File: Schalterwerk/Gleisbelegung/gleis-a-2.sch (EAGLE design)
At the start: 24 parts, among them Q1 P-MOSFET, Q2 P-MOSFET, X1 PHNX_4P_508CONN_1017493, X3 IO-HAT, X4 RJ45-JACK, X5 PHNX_4P_350CONN_1984989_PXC, X6 PHNX_4P_350CONN_1984989_PXC

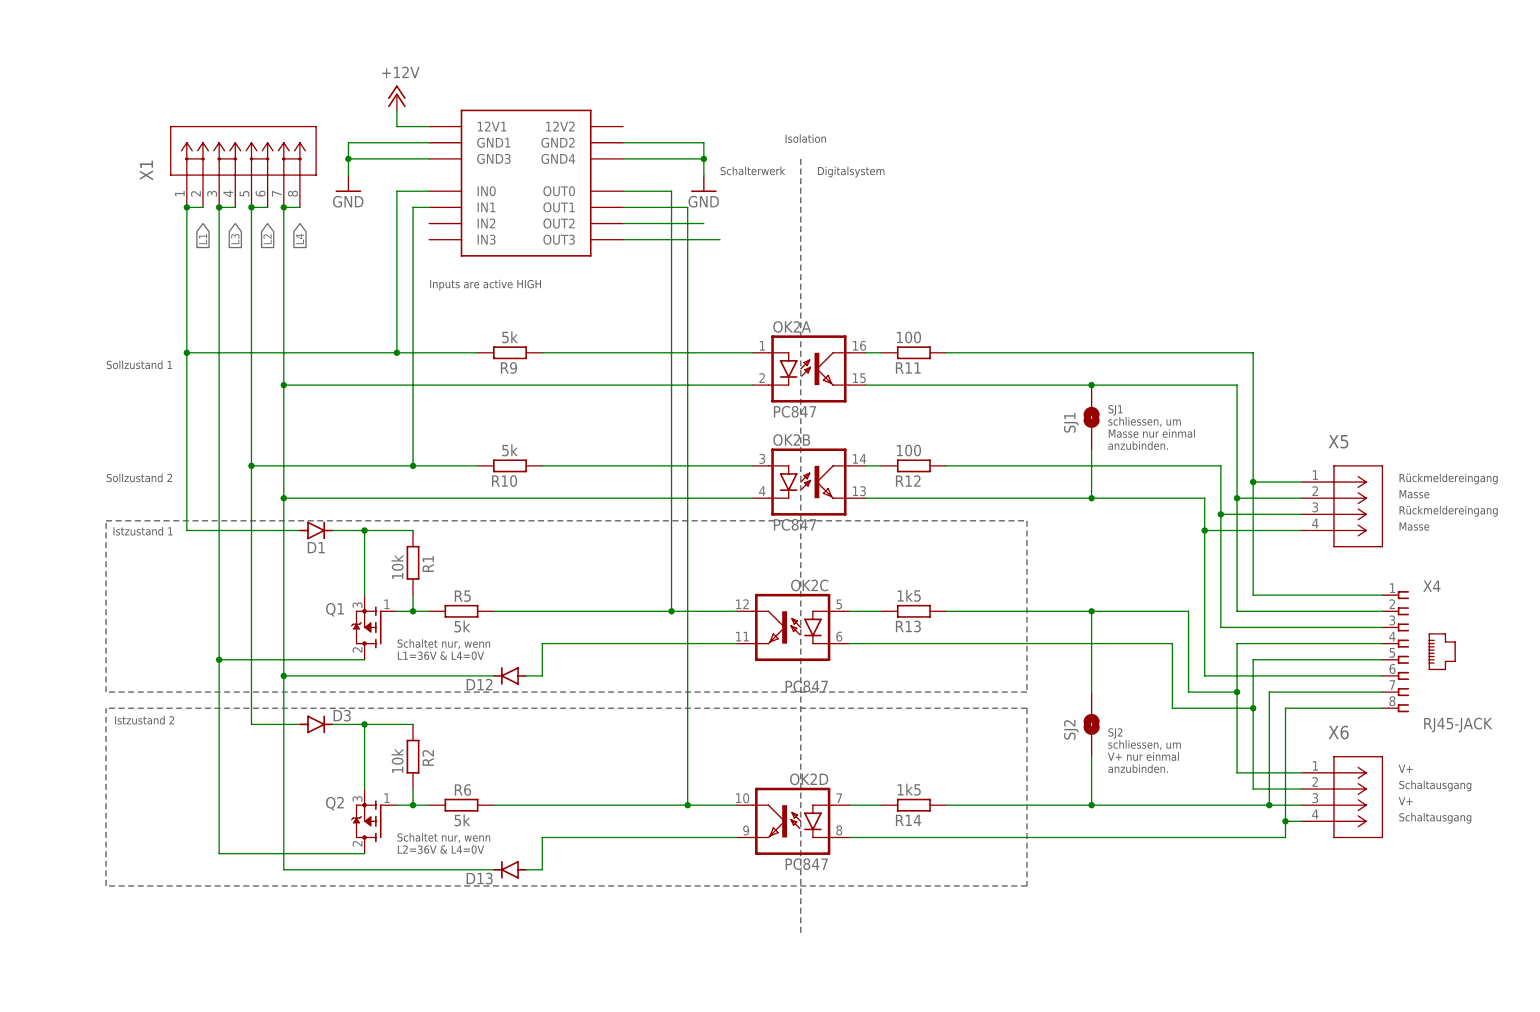
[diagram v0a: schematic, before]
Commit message: Renumbers the schematic so that the digitalsystem side can be copy-pasted between layouts.
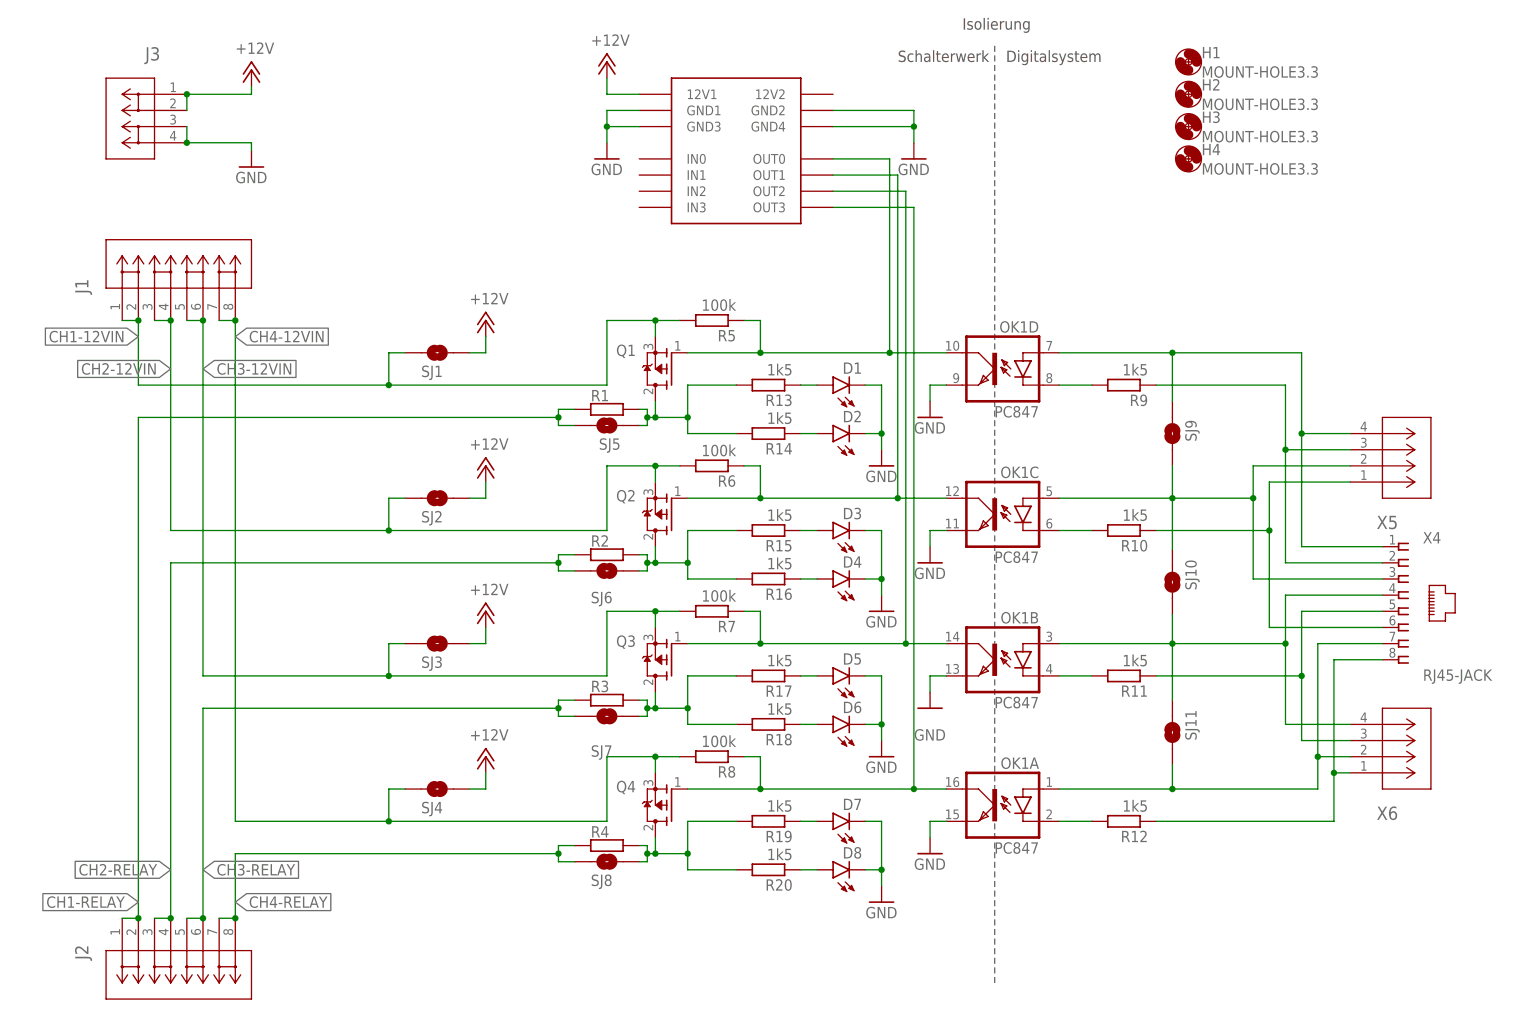
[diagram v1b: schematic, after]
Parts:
- removed D12, D13: (no value), diode:DIODE-MINIMELF
- removed OK2: PC847, optocoupler:PC847
- removed X1: PHNX_4P_508CONN_1017493, eagleparts:PHNX_4P_508CONN_1017493
- removed X3: IO-HAT, eagleparts:IO-HAT
- added D2, D4, D6, D8: LEDHEADER, eagleparts:LEDHEADER
- added D5, D7: (no value), led:LEDCHIPLED_0603
- added H1, H2, H3, H4: MOUNT-HOLE3.3, holes:MOUNT-HOLE3.3
- added J1, J2: PHNX_4P_508CONN_1017493, eagleparts:PHNX_4P_508CONN_1017493
- added J3: PHNX_2P_508CONN_1017491, eagleparts:PHNX_2P_508CONN_1017491
- added OK1: PC847, optocoupler:PC847
- added Q3, Q4: P-MOSFET, eagleparts:P-MOSFET
- added R15, R16, R17, R18, R19, R20: 1k5, rcl:R-EU_R0805
- added R3, R4: (no value), rcl:R-EU_VTA52
- added R7, R8: 100k, rcl:R-EU_R0805
- added SJ10, SJ11, SJ3, SJ4, SJ5, SJ6, SJ7, SJ8, SJ9: (no value), eagleparts:SJRND2
- added X2: IO-HAT, eagleparts:IO-HAT
- D1, D3: device diode:DIODE-DO214AC -> led:LEDCHIPLED_0603
- R1, R2: value 10k -> (none); device rcl:R-EU_R0805 -> rcl:R-EU_VTA52
- R10, R9: value 5k -> 1k5
- R11, R12: value 100 -> 1k5
- R5, R6: value 5k -> 100k
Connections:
- removed net L1: D1.A, R9.2, X1.1, X1.2, X3G$1.IN0
- removed net L2: D3.A, R10.2, X1.5, X1.6, X3G$1.IN1
- removed net L3: Q1.D, Q2.D, X1.3, X1.4
- removed net L4: D12.C, D13.C, OK2A.C, OK2B.C, X1.7, X1.8
- removed net N$15: OK2C.COL, R5.2, X3G$1.OUT0
- removed net N$16: OK2D.COL, R6.2, X3G$1.OUT1
- removed net N$22: D13.A, OK2D.EMIT
- removed net NX41: R11.1, X4.1, X5.1
- removed net NX42: OK2A.EMIT, SJ1.2, X4.2, X5.2
- removed net NX43: R12.1, X4.3, X5.3
- removed net NX44: R13.1, SJ2.2, X4.4, X6.1
- removed net NX45: OK2C.C, X4.5, X6.2
- removed net NX46: OK2B.EMIT, SJ1.1, X4.6, X5.4
- removed net NX47: R14.1, SJ2.1, X4.7, X6.3
- removed net NX48: OK2D.C, X4.8, X6.4
- new net CH1-12VIN: J1.1, J1.2, Q1.S, R5.2, SJ1.1
- new net CH1-RELAY: J2.1, J2.2, R1.1, SJ5.1
- new net CH2-12VIN: J1.3, J1.4, Q2.S, R6.2, SJ2.1
- new net CH2-RELAY: J2.3, J2.4, R2.1, SJ6.1
- new net CH3-12VIN: J1.5, J1.6, Q3.S, R7.2, SJ3.1
- new net CH3-RELAY: J2.5, J2.6, R3.1, SJ7.1
- new net CH4-12VIN: J1.7, J1.8, Q4.S, R8.2, SJ4.1
- new net CH4-RELAY: J2.7, J2.8, R4.1, SJ8.1
- new net N$10: Q2.D, R15.2, R16.2, R2.2, SJ6.2
- new net N$11: Q3.D, R17.2, R18.2, R3.2, SJ7.2
- new net N$18: OK1C.C, R10.2
- new net N$23: D3.A, R15.1
- new net N$27: D6.A, R18.1
- new net N$29: D7.A, R19.1
- new net N$30: D8.A, R20.1
- new net X41: OK1D.A, SJ9.2, X4.1, X5.4
- new net X42: R9.1, X4.2, X5.3
- new net X43: OK1C.A, SJ10.2, SJ9.1, X4.3, X5.2
- new net X44: OK1B.A, SJ10.1, SJ11.2, X4.4, X6.4
- new net X45: R11.1, X4.5, X6.3
- new net X46: R10.1, X4.6, X5.1
- new net X47: OK1A.A, SJ11.1, X4.7, X6.2
- new net X48: R12.1, X4.8, X6.1
- net +12V: now also J3.1, J3.2, SJ1.2, SJ2.2, SJ3.2, SJ4.2, X2G$1.12V1; no longer X3G$1.12V1
- net GND: now also D1.C, D2.C, D3.C, D4.C, D5.C, D6.C, D7.C, D8.C, J3.3, J3.4, OK1A.EMIT, OK1B.EMIT, OK1C.EMIT, OK1D.EMIT, X2G$1.GND1, X2G$1.GND2, X2G$1.GND3, X2G$1.GND4; no longer X3G$1.GND1, X3G$1.GND2, X3G$1.GND3, X3G$1.GND4
- net N$1: now also Q1.D, R1.2, R13.2, R14.2, SJ5.2; no longer D3.C, Q2.S, R2.1
- net N$12: now also OK1A.COL, Q4.G, R8.1, X2G$1.OUT3; no longer Q2.G, R2.2, R6.1
- net N$13: now also Q4.D, R19.2, R20.2, R4.2, SJ8.2; no longer D1.C, Q1.S, R1.1
- net N$17: now also OK1D.C, R9.2; no longer D12.A, OK2C.EMIT
- net N$19: now also OK1A.C, R12.2; no longer OK2A.COL, R11.2
- net N$2: now also OK1C.COL, Q2.G, R6.1, X2G$1.OUT1; no longer OK2A.A, R9.1
- net N$21: now also D2.A, R14.1; no longer OK2B.COL, R12.2
- net N$24: now also D4.A, R16.1; no longer X3G$1.OUT2
- net N$25: now also D5.A, R17.1; no longer X3G$1.OUT3
- net N$5: now also OK1B.COL, Q3.G, R7.1, X2G$1.OUT2; no longer OK2C.A, R13.2
- net N$7: now also OK1B.C, R11.2; no longer OK2B.A, R10.1
- net N$8: now also D1.A, R13.1; no longer OK2D.A, R14.2
- net N$9: now also OK1D.COL, X2G$1.OUT0; no longer R1.2
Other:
- note added: "Isolierung"
- note removed: "Inputs are active HIGH"
- note removed: "Isolation"
- note removed: "Istzustand 1"
- note removed: "Istzustand 2"
- note removed: "Masse"
- note removed: "Rückmeldereingang"
- note removed: "SJ1 schliessen, um Masse nur einmal anzubinden."
- note removed: "SJ2 schliessen, um V+ nur einmal anzubinden."
- note removed: "Schaltausgang"
- note removed: "Schaltet nur, wenn L1=36V & L4=0V"
- note removed: "Schaltet nur, wenn L2=36V & L4=0V"
- note removed: "Sollzustand 1"
- note removed: "Sollzustand 2"
- note removed: "V+"
- moved on the sheet: Q1, Q2, R1, R10, R11, R12, R13, R14, R2, R5, R6, R9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

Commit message: Renames signals on X4 again
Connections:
- net X41 renamed NX41
- net X42 renamed NX42
- net X43 renamed NX43
- net X44 renamed NX44
- net X45 renamed NX45
- net X46 renamed NX46
- net X47 renamed NX47
- net X48 renamed NX48
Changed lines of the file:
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@@
 </segment>
 </net>
-<net name="X41" class="0">
+<net name="NX41" class="0">
 <segment>
 <pinref part="OK1" gate="D" pin="A"/>
@@
 </segment>
 </net>
-<net name="X42" class="0">
+<net name="NX42" class="0">
 <segment>
 <pinref part="R9" gate="G$1" pin="1"/>
@@
 </segment>
 </net>
-<net name="X43" class="0">
+<net name="NX43" class="0">
 <segment>
 <pinref part="OK1" gate="C" pin="A"/>
@@
 </segment>
 </net>
-<net name="X45" class="0">
+<net name="NX45" class="0">
 <segment>
 <pinref part="R11" gate="G$1" pin="1"/>
@@
 </segment>
 </net>
-<net name="X47" class="0">
+<net name="NX47" class="0">
 <segment>
 <pinref part="X4" gate="G$1" pin="7"/>
@@
 </segment>
 </net>
-<net name="X48" class="0">
+<net name="NX48" class="0">
 <segment>
 <pinref part="R12" gate="G$1" pin="1"/>
@@
 </segment>
 </net>
-<net name="X46" class="0">
+<net name="NX46" class="0">
 <segment>
 <pinref part="R10" gate="G$1" pin="1"/>
@@
 </segment>
 </net>
-<net name="X44" class="0">
+<net name="NX44" class="0">
 <segment>
 <pinref part="OK1" gate="B" pin="A"/>
